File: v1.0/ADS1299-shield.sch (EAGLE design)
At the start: 31 parts, among them IC1 ADS1298*PAG*, IC2 TPS73250DBVT, IC3 TPS73233DBVT

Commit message: schematic work - power supplies and decoupling done; updated ADS1299 library symbol to better organize pinouts; minor updates to power supply libraries
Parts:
- removed IC1: ADS1298*PAG*, burr-brown-5a:ADS1298*PAG*
- removed JP1, JP2: M24, SparkFun-Connectors:M24
- added C15: 2.2uF, SparkFun-Passives:CAP0603-CAP
- added C16: 10 uF, SparkFun-Passives:CAP0603-CAP
- added C26, C28, C29, C30: 1uF, SparkFun-Passives:CAP0603-CAP
- added C27: 10uf, SparkFun-Passives:CAP0603-CAP
- added L3, L4: 3.3 uH, SparkFun-Passives:INDUCTOR0603
- added U$2: TPS604XXDBV, TPS604xx:TPS604XXDBV
- added U$3: ADS1299*PAG*, ADS129x:ADS1299*PAG*
- C17: value 22uF -> 100uF
- C24: value 100pF -> 10uf
- IC2: value TPS73250DBVT -> TPS73225DBVT
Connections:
- removed net PACEOUT1: IC1.PACE_OUT1, JP2.6
- removed net PACEOUT2: IC1.PACE_OUT2, JP2.7
- removed net RLD_IN: IC1.RLD_IN, JP1.22
- removed net RLD_INV: C25.2, IC1.RLD_INV, R1.2
- removed net RLD_OUT: C25.1, IC1.RLD_OUT, R1.1
- removed net RLD_REF: IC1.RLD_REF, JP1.21
- removed net VCC: IC2.EN, IC2.IN, IC3.EN, IC3.IN, JP1.25, JP2.25
- new net AVSS: C11.2, C12.2, C29.2, C30.2, U$3.AVSS1, U$3.AVSS@1, U$3.AVSS@2, U$3.AVSS@3, U$3.AVSS@4, U$3.AVSS@5
- new net BIASIN: U$3.BIASIN
- new net BIASINV: C25.2, R1.2, U$3.BIASINV
- new net BIASOUT: C25.1, R1.1, U$3.BIASOUT
- new net BIASREF: U$3.BIASREF
- new net GND: C27.1, C28.1, C7.2, C8.2, IC2.EN, IC2.IN, IC3.EN, IC3.IN, L4.1
- new net N$10: C26.1, U$2.CFLY_N
- new net N$12: L4.2, U$2.IN
- new net N$9: C26.2, U$2.CFLY_P
- new net SRB1: U$3.SRB2
- new net SRB2: U$3.SRB1
- new net VCC_-5V: C24.1, L3.2
- net !PWDN: now also U$3.!PWDN; no longer IC1.!PWDN, JP2.9
- net !RESET: now also U$3.!RESET; no longer IC1.!RESET, JP2.10
- net AGND: now also C15.2, C16.2, C27.2, C28.2, C29.1, C30.1, U$2.GND, U$3.DGND@1, U$3.DGND@2, U$3.DGND@3, U$3.VREFN; no longer C11.2, C12.2, C7.2, C8.2, IC1.AVSS1, IC1.AVSS_1, IC1.AVSS_2, IC1.AVSS_3, IC1.AVSS_4, IC1.AVSS_5, IC1.DGND_1, IC1.DGND_2, IC1.DGND_3, IC1.RESV1, IC1.VREFN, JP1.2, JP1.23, JP1.3, JP1.4, JP2.2, JP2.3, JP2.4
- net AVDD: now also U$3.AVDD@1, U$3.AVDD@2, U$3.AVDD@3, U$3.AVDD@4, U$3.AVDD@5, U$3.AVDD@6; no longer IC1.AVDD1, IC1.AVDD_1, IC1.AVDD_2, IC1.AVDD_3, IC1.AVDD_4, IC1.AVDD_5, JP1.24, JP2.24
- net CLK: now also U$3.CLK; no longer IC1.CLK, JP2.11
- net CLKSEL: now also U$3.CLKSEL; no longer IC1.CLKSEL, JP2.12
- net DAISY_IN: now also U$3.DAISY_IN; no longer IC1.DAISY_IN, JP2.8
- net DVDD: now also U$3.DVDD@1, U$3.DVDD@2; no longer IC1.DVDD_1, IC1.DVDD_2, JP2.23
- net GPIO1: now also U$3.GPIO1; no longer IC1.GPIO1, JP2.22
- net GPIO2: now also U$3.GPIO2; no longer IC1.GPIO2, JP2.21
- net GPIO3: now also U$3.GPIO3; no longer IC1.GPIO3, JP2.20
- net GPIO4: now also U$3.GPIO4; no longer IC1.GPIO4, JP2.19
- net IN1N: now also U$3.IN1N; no longer IC1.IN1N, JP1.19
- net IN1P: now also U$3.IN1P; no longer IC1.IN1P, JP1.20
- net IN2N: now also U$3.IN2N; no longer IC1.IN2N, JP1.17
- net IN2P: now also U$3.IN2P; no longer IC1.IN2P, JP1.18
- net IN3N: now also U$3.IN3N; no longer IC1.IN3N, JP1.15
- net IN3P: now also U$3.IN3P; no longer IC1.IN3P, JP1.16
- net IN4N: now also U$3.IN4N; no longer IC1.IN4N, JP1.13
- net IN4P: now also U$3.IN4P; no longer IC1.IN4P, JP1.14
- net IN5N: now also U$3.IN5N; no longer IC1.IN5N, JP1.11
- net IN5P: now also U$3.IN5P; no longer IC1.IN5P, JP1.12
- net IN6N: now also U$3.IN6N; no longer IC1.IN6N, JP1.9
- net IN6P: now also U$3.IN6P; no longer IC1.IN6P, JP1.10
- net IN7N: now also U$3.IN7N; no longer IC1.IN7N, JP1.7
- net IN7P: now also U$3.IN7P; no longer IC1.IN7P, JP1.8
- net IN8N: now also U$3.IN8N; no longer IC1.IN8N, JP1.5
- net IN8P: now also U$3.IN8P; no longer IC1.IN8P, JP1.6
- net N$3: now also U$3.VCAP1; no longer IC1.VCAP1
- net N$4: now also U$3.VCAP2; no longer IC1.VCAP2
- net N$5: now also U$3.VCAP3; no longer IC1.VCAP3
- net N$7: now also C15.1, C16.1, L3.1, U$2.OUT; no longer C24.1, IC1.WCT
- net N$8: now also U$3.VCAP4; no longer IC1.VCAP4
- net SPI_CLK: now also U$3.SCLK; no longer IC1.SCLK, JP2.17
- net SPI_CS: now also U$3.!CS; no longer IC1.!CS, JP2.14
- net SPI_DRDY: now also U$3.!DRDY; no longer IC1.!DRDY, JP2.18
- net SPI_IN: now also U$3.DIN; no longer IC1.DIN, JP2.16
- net SPI_OUT: now also U$3.DOUT; no longer IC1.DOUT, JP2.15
- net SPI_START: now also U$3.START; no longer IC1.START, JP2.13
- net VREFP: now also U$3.VREFP; no longer IC1.VREFP, JP2.5
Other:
- note added: "Decoupling"
- note added: "v1.0"
- note removed: "v0.1"

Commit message: updated ads1299 library to have NAME and VALUE; improved power supply section, including supply-select jumpers
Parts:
- added C31, C32: 1uF, SparkFun-Passives:CAP0603-CAP
- added C33: 0.1uF, SparkFun-Passives:CAP0603-CAP
- added JP1: AVDD_5V-2.5V, SparkFun-Passives:JUMPER-3PTH
- added JP2: AVSS_-2.5V-GND, SparkFun-Passives:JUMPER-3PTH
- IC2: value TPS73225DBVT -> TPS72325DBVT
- IC3: value TPS73233DBVT -> TPS73225DBVT
- U1: value ADS1299*PAG* -> ADS1299IPAG
- renumbered U$3 to U1
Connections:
- new net +2.5V: C6.1, JP1.3, L2.2
- new net -2.5V: C3.1, JP2.1, L1.2
- new net N$11: C32.1, IC3.NR/FB
- new net N$13: C31.1, IC2.NR/FB
- new net VCC_5V: C27.1, IC3.EN, IC3.IN, JP1.1, L4.1
- net AGND: now also C31.2, C32.2, JP2.3
- net AVDD: now also C33.1, JP1.2; no longer C3.1, L1.2
- net AVSS: now also C33.2, JP2.2
- net DVDD: no longer C6.1, L2.2
- net GND: no longer C27.1, C28.1, IC2.EN, IC2.IN, IC3.EN, IC3.IN, L4.1
- net VCC_-5V: now also C28.1, IC2.EN, IC2.IN
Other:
- note added: "Analog-Digital Converter"
- note added: "Power"
- moved on the sheet: C1, C10, C11, C12, C13, C14, C15, C16, C2, C24, C26, C27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

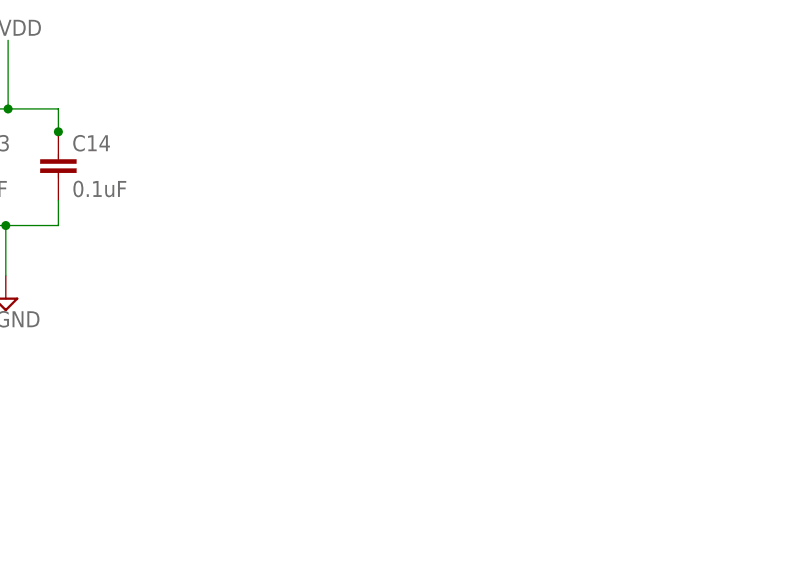
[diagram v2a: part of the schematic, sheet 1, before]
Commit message: input filtering section done
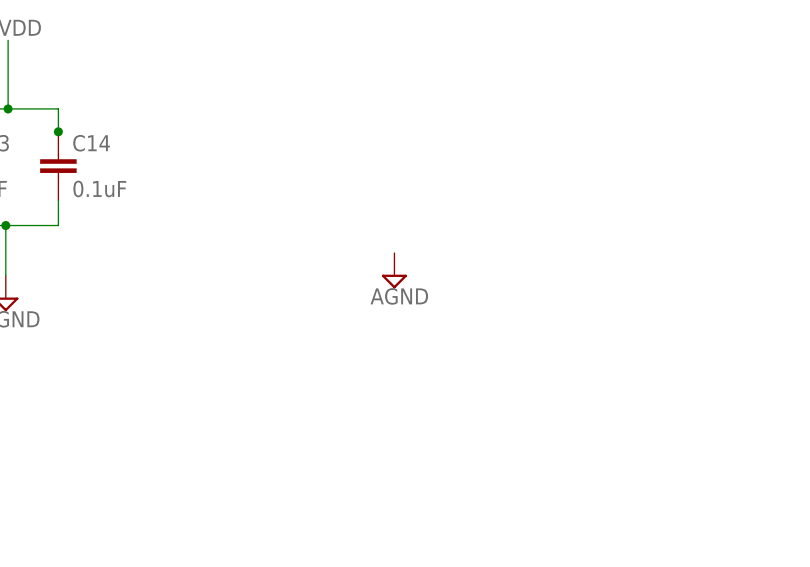
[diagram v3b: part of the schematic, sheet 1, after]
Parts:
- added C34, C35, C36, C37, C38, C39, C40, C41, C42, C43, C44, C45, C46, C47, C48, C49: 4.7nF, SparkFun-Passives:CAP0603-CAP
- added R10, R11, R12, R13, R14, R15, R16, R17, R2, R3, R4, R5, R6, R7, R8, R9: 4.99k, SparkFun-Passives:RESISTOR0603-RES
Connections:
- new net AIN1N: C34.2, C37.2, C43.2, R11.2, R2.2, R5.2
- new net AIN1P: C35.1, C36.1, R3.2, R4.2
- new net AIN3N: C39.2, R7.2
- new net AIN3P: C38.1, R6.2
- new net AIN4N: C41.2, R9.2
- new net AIN4P: C40.1, R8.2
- new net AIN5P: C42.1, R10.2
- new net AIN6N: C45.2, R13.2
- new net AIN6P: C44.1, R12.2
- new net AIN7N: C47.2, R15.2
- new net AIN7P: C46.1, R14.2
- new net AIN8N: C49.2, R17.2
- new net AIN8P: C48.1, R16.2
- net AGND: now also C34.1, C35.2, C36.2, C37.1, C38.2, C39.1, C40.2, C41.1, C42.2, C43.1, C44.2, C45.1, C46.2, C47.1, C48.2, C49.1
- net IN1N: now also R2.1, R5.1
- net IN1P: now also R3.1, R4.1
- net IN2N: now also R7.1
- net IN3P: now also R6.1
- net IN4N: now also R9.1
- net IN4P: now also R8.1
- net IN5N: now also R11.1
- net IN5P: now also R10.1
- net IN6N: now also R13.1
- net IN6P: now also R12.1
- net IN7N: now also R15.1
- net IN7P: now also R14.1
- net IN8N: now also R17.1
- net IN8P: now also R16.1
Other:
- note added: "Input Filtering"

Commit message: configuration jumpers added but not done; EEPROM in and finished; level shifters finished
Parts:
- added C52, C54, C56, C58: 1uF, SparkFun-Passives:CAP0603-CAP
- added C53, C55, C57, C59: 0.1uF, SparkFun-Passives:CAP0603-CAP
- added D2: RED, SparkFun-LED:LED-RED1206
- added IC1: 24AA256UID, microchip:24LC256SN
- added JP3, JP4: (no value), adafruit:PINHD-1X3CB
- added JP5: (no value), pin-headers:PINHD-2X10
- added JP6: (no value), pin-headers:PINHD-2X12
- added R18: 270, SparkFun-Passives:RESISTOR0603-RES
- added R19, R20, R21: 10k, SparkFun-Passives:RESISTOR0603-RES
- added U2, U3: TXB0108PWR, adafruit:TXB0108PWR
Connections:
- removed net SPI_DRDY: U1.!DRDY
- removed net SPI_START: U1.START
- new net !ADS_PWDN: U2.B8
- new net !ADS_RESET: U3.B1
- new net !SPI_CS: U1.!CS
- new net ADS_CLK: U2.B7
- new net ADS_CLKSEL: U2.B6
- new net ADS_DRDY: U2.B1
- new net ADS_SPI_CLK: U2.B3
- new net ADS_SPI_CS: U2.B2
- new net ADS_SPI_IN: U2.B4
- new net ADS_SPI_OUT: U2.B5
- new net ADS_START: U3.B2
- new net ARD_UNUSED@1: U3.B3
- new net ARD_UNUSED@2: U3.B4
- new net ARD_UNUSED@3: U3.B5
- new net ARD_UNUSED@4: U3.B6
- new net ARD_UNUSED@5: U3.B7, U3.B8
- new net BOARD_ADDR_0: IC1.A0, JP6.23, R19.2
- new net BOARD_ADDR_1: IC1.A1, JP6.21, R20.2
- new net BOARD_ADDR_2: IC1.A2, R21.2
- new net DRDY: U1.!DRDY, U2.A1
- new net DVDD1: C56.2, C57.2, U3.VCCA
- new net IOREF: C54.2, C55.2, U2.VCCB
- new net IOREF1: C58.2, C59.2, U3.VCCB
- new net N$14: D2.A, R18.2
- new net SCL1: IC1.SCL
- new net SDA1: IC1.SDA
- new net START: U1.START, U3.A2
- new net UNUSED@1: U3.A3
- new net UNUSED@2: U3.A4
- new net UNUSED@3: U3.A5, U3.A6
- new net UNUSED@4: U3.A7
- new net UNUSED@5: U3.A8
- net !PWDN: now also U2.A8
- net !RESET: now also U3.A1
- net AGND: now also C52.1, C53.1, C54.1, C55.1, C56.1, C57.1, C58.1, C59.1, D2.C, IC1.GND, IC1.WP, R19.1, R20.1, R21.1, U2.GND, U3.GND
- net CLK: now also U2.A7
- net CLKSEL: now also U2.A6
- net DVDD: now also C52.2, C53.2, IC1.VCC, JP6.22, JP6.24, U2.VCCA
- net GPIO4: now also R18.1
- net SPI_CLK: now also U2.A3
- net SPI_CS: now also U2.A2; no longer U1.!CS
- net SPI_IN: now also U2.A4
- net SPI_OUT: now also U2.A5
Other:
- note added: "ADC Decoupling"
- note added: "Configuration jumpers"
- note added: "GPIO LED"
- note added: "Level Shifting"
- note added: "UID-capable Settings EEPROM"
- note removed: "Decoupling"
